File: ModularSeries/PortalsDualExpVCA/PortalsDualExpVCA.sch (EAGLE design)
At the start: 71 parts, among them Q1 2N3906, Q2 2N3906, Q3 2N3906, Q4 2N3906

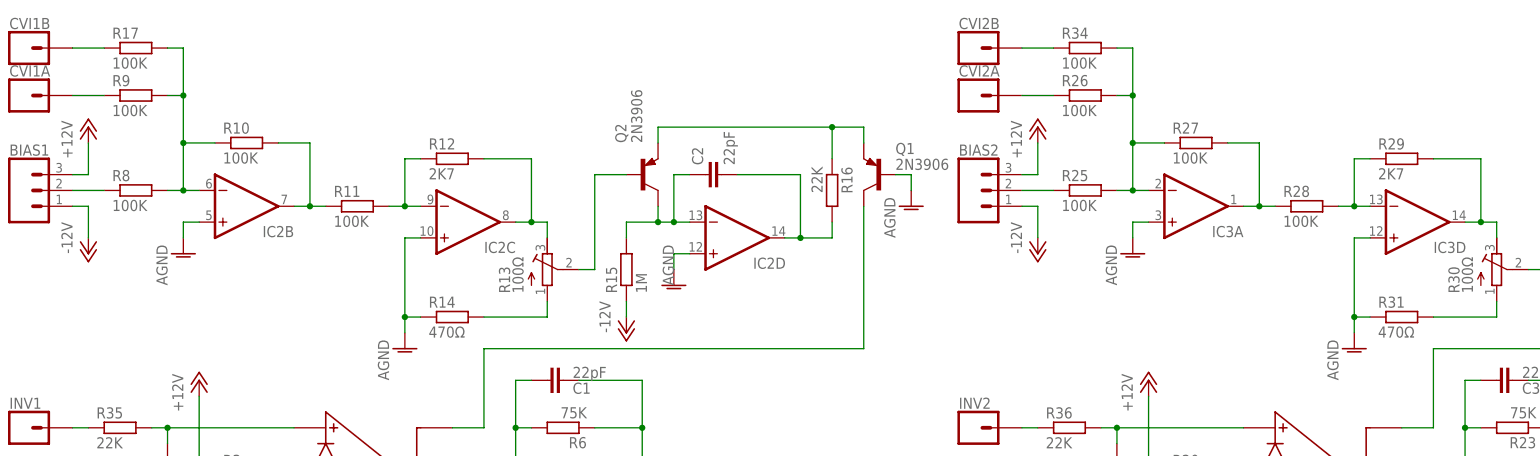
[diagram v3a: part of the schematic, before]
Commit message: Control PCBs for Prism, Portals, TimeSeeds and Knives added
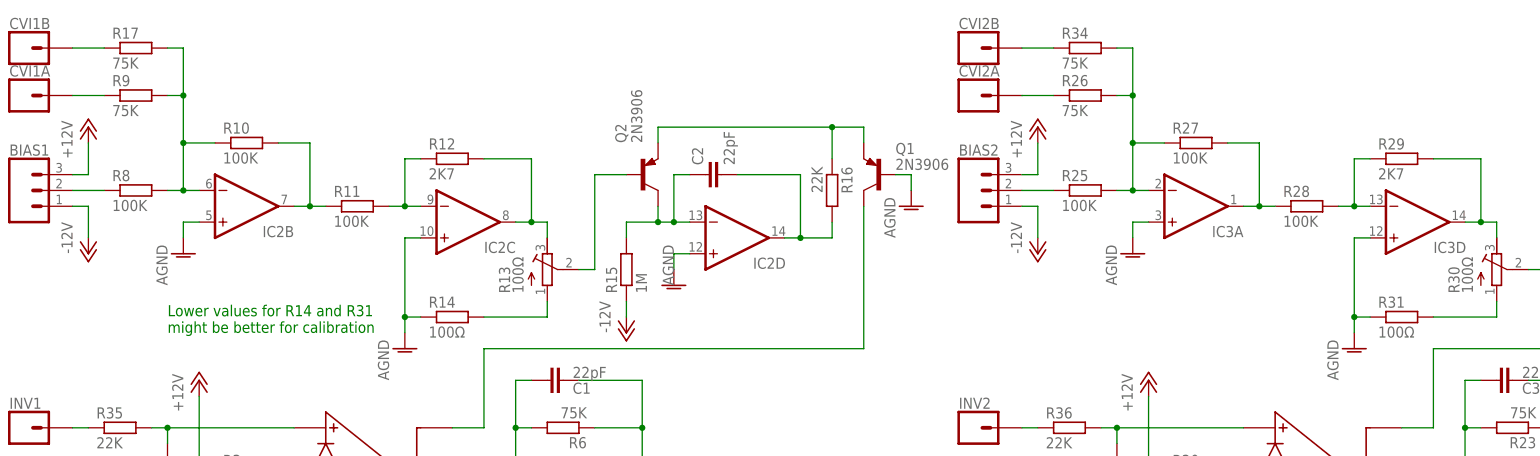
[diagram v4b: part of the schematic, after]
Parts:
- R14, R31: value 470Ω -> 100Ω
- R17, R26, R34, R9: value 100K -> 75K
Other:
- note added: "Lower values for R14 and R31 might be better for calibration"
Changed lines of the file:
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@@
 <part name="CVI1A" library="ElectricNoodleBox" deviceset="1XWIREPAD" device=""/>
 <part name="R8" library="rcl" library_urn="urn:adsk.eagle:library:334" deviceset="R-EU_" device="0207/10" package3d_urn="urn:adsk.eagle:package:23491/2" value="100K"/>
-<part name="R9" library="rcl" library_urn="urn:adsk.eagle:library:334" deviceset="R-EU_" device="0207/10" package3d_urn="urn:adsk.eagle:package:23491/2" value="100K"/>
+<part name="R9" library="rcl" library_urn="urn:adsk.eagle:library:334" deviceset="R-EU_" device="0207/10" package3d_urn="urn:adsk.eagle:package:23491/2" value="75K"/>
 <part name="R10" library="rcl" library_urn="urn:adsk.eagle:library:334" deviceset="R-EU_" device="0207/10" package3d_urn="urn:adsk.eagle:package:23491/2" value="100K"/>
 <part name="R11" library="rcl" library_urn="urn:adsk.eagle:library:334" deviceset="R-EU_" device="0207/10" package3d_urn="urn:adsk.eagle:package:23491/2" value="100K"/>
@@
 <part name="AGND5" library="supply1" library_urn="urn:adsk.eagle:library:371" deviceset="AGND" device=""/>
 <part name="R13" library="rcl" library_urn="urn:adsk.eagle:library:334" deviceset="R-TRIMM" device="3296W" package3d_urn="urn:adsk.eagle:package:26033/1" value="100Ω"/>
-<part name="R14" library="rcl" library_urn="urn:adsk.eagle:library:334" deviceset="R-EU_" device="0207/10" package3d_urn="urn:adsk.eagle:package:23491/2" value="470Ω"/>
+<part name="R14" library="rcl" library_urn="urn:adsk.eagle:library:334" deviceset="R-EU_" device="0207/10" package3d_urn="urn:adsk.eagle:package:23491/2" value="100Ω"/>
 <part name="AGND6" library="supply1" library_urn="urn:adsk.eagle:library:371" deviceset="AGND" device=""/>
 <part name="R15" library="rcl" library_urn="urn:adsk.eagle:library:334" deviceset="R-EU_" device="0207/10" package3d_urn="urn:adsk.eagle:package:23491/2" value="1M"/>
@@
 <part name="P+3" library="supply1" library_urn="urn:adsk.eagle:library:371" deviceset="+12V" device=""/>
 <part name="P-3" library="supply1" library_urn="urn:adsk.eagle:library:371" deviceset="-12V" device=""/>
-<part name="R17" library="rcl" library_urn="urn:adsk.eagle:library:334" deviceset="R-EU_" device="0207/10" package3d_urn="urn:adsk.eagle:package:23491/2" value="100K"/>
+<part name="R17" library="rcl" library_urn="urn:adsk.eagle:library:334" deviceset="R-EU_" device="0207/10" package3d_urn="urn:adsk.eagle:package:23491/2" value="75K"/>
 <part name="CVI1B" library="ElectricNoodleBox" deviceset="1XWIREPAD" device=""/>
 <part name="SI2" library="ElectricNoodleBox" deviceset="1XWIREPAD" device=""/>
@@
 <part name="CVI2A" library="ElectricNoodleBox" deviceset="1XWIREPAD" device=""/>
 <part name="R25" library="rcl" library_urn="urn:adsk.eagle:library:334" deviceset="R-EU_" device="0207/10" package3d_urn="urn:adsk.eagle:package:23491/2" value="100K"/>
-<part name="R26" library="rcl" library_urn="urn:adsk.eagle:library:334" deviceset="R-EU_" device="0207/10" package3d_urn="urn:adsk.eagle:package:23491/2" value="100K"/>
+<part name="R26" library="rcl" library_urn="urn:adsk.eagle:library:334" deviceset="R-EU_" device="0207/10" package3d_urn="urn:adsk.eagle:package:23491/2" value="75K"/>
 <part name="R27" library="rcl" library_urn="urn:adsk.eagle:library:334" deviceset="R-EU_" device="0207/10" package3d_urn="urn:adsk.eagle:package:23491/2" value="100K"/>
 <part name="R28" library="rcl" library_urn="urn:adsk.eagle:library:334" deviceset="R-EU_" device="0207/10" package3d_urn="urn:adsk.eagle:package:23491/2" value="100K"/>
@@
 <part name="AGND11" library="supply1" library_urn="urn:adsk.eagle:library:371" deviceset="AGND" device=""/>
 <part name="R30" library="rcl" library_urn="urn:adsk.eagle:library:334" deviceset="R-TRIMM" device="3296W" package3d_urn="urn:adsk.eagle:package:26033/1" value="100Ω"/>
-<part name="R31" library="rcl" library_urn="urn:adsk.eagle:library:334" deviceset="R-EU_" device="0207/10" package3d_urn="urn:adsk.eagle:package:23491/2" value="470Ω"/>
+<part name="R31" library="rcl" library_urn="urn:adsk.eagle:library:334" deviceset="R-EU_" device="0207/10" package3d_urn="urn:adsk.eagle:package:23491/2" value="100Ω"/>
 <part name="AGND12" library="supply1" library_urn="urn:adsk.eagle:library:371" deviceset="AGND" device=""/>
 <part name="R32" library="rcl" library_urn="urn:adsk.eagle:library:334" deviceset="R-EU_" device="0207/10" package3d_urn="urn:adsk.eagle:package:23491/2" value="1M"/>
@@
 <part name="P+5" library="supply1" library_urn="urn:adsk.eagle:library:371" deviceset="+12V" device=""/>
 <part name="P-5" library="supply1" library_urn="urn:adsk.eagle:library:371" deviceset="-12V" device=""/>
-<part name="R34" library="rcl" library_urn="urn:adsk.eagle:library:334" deviceset="R-EU_" device="0207/10" package3d_urn="urn:adsk.eagle:package:23491/2" value="100K"/>
+<part name="R34" library="rcl" library_urn="urn:adsk.eagle:library:334" deviceset="R-EU_" device="0207/10" package3d_urn="urn:adsk.eagle:package:23491/2" value="75K"/>
 <part name="CVI2B" library="ElectricNoodleBox" deviceset="1XWIREPAD" device=""/>
 <part name="C5" library="rcl" library_urn="urn:adsk.eagle:library:334" deviceset="C-EU" device="050-025X075" package3d_urn="urn:adsk.eagle:package:23637/1" value="100nF"/>
@@
 <text x="177.8" y="22.86" size="1.778" layer="91">Ground terminals
 for jacks / pots</text>
+<text x="30.48" y="88.9" size="1.778" layer="91">Lower values for R14 and R31
+might be better for calibration</text>
 </plain>
 <instances>

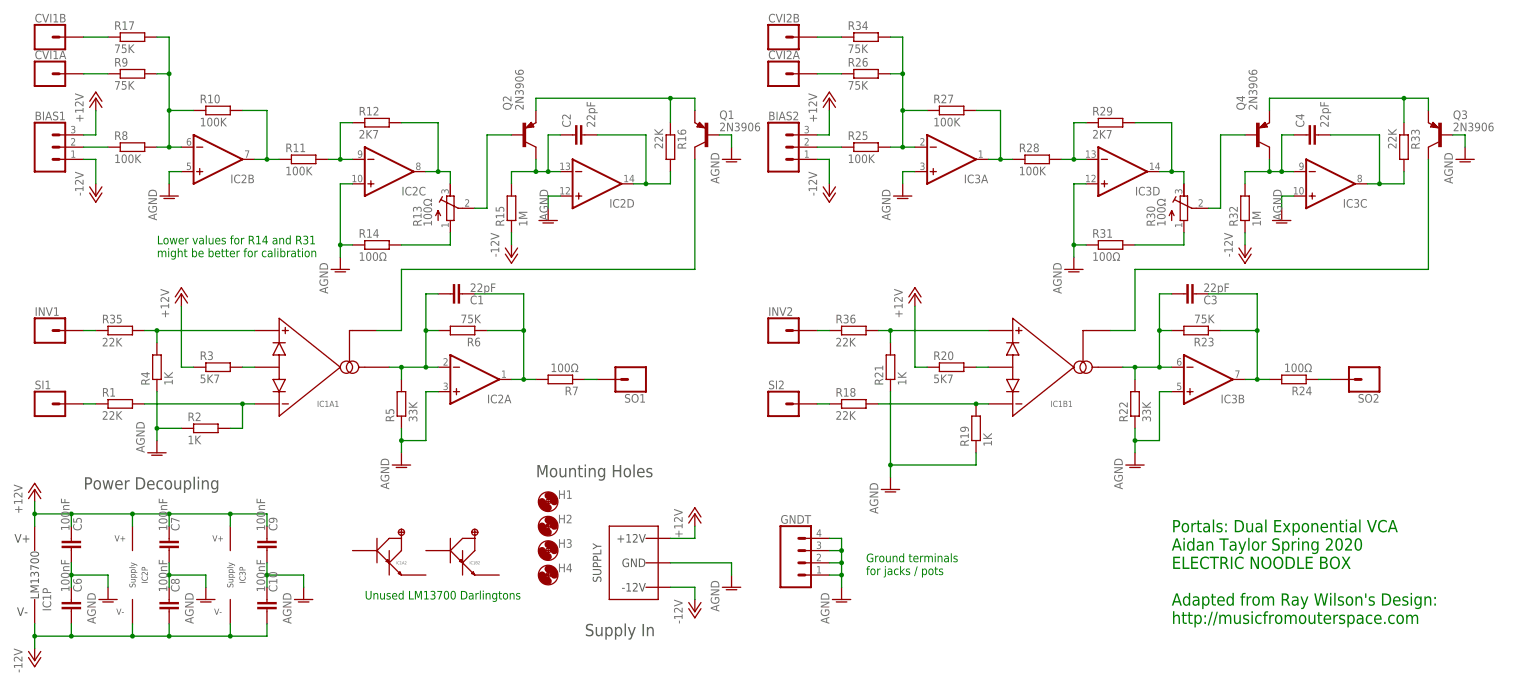
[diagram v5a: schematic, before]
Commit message: Updates to Portals and Knives, Panel layout for Prism and Knives added
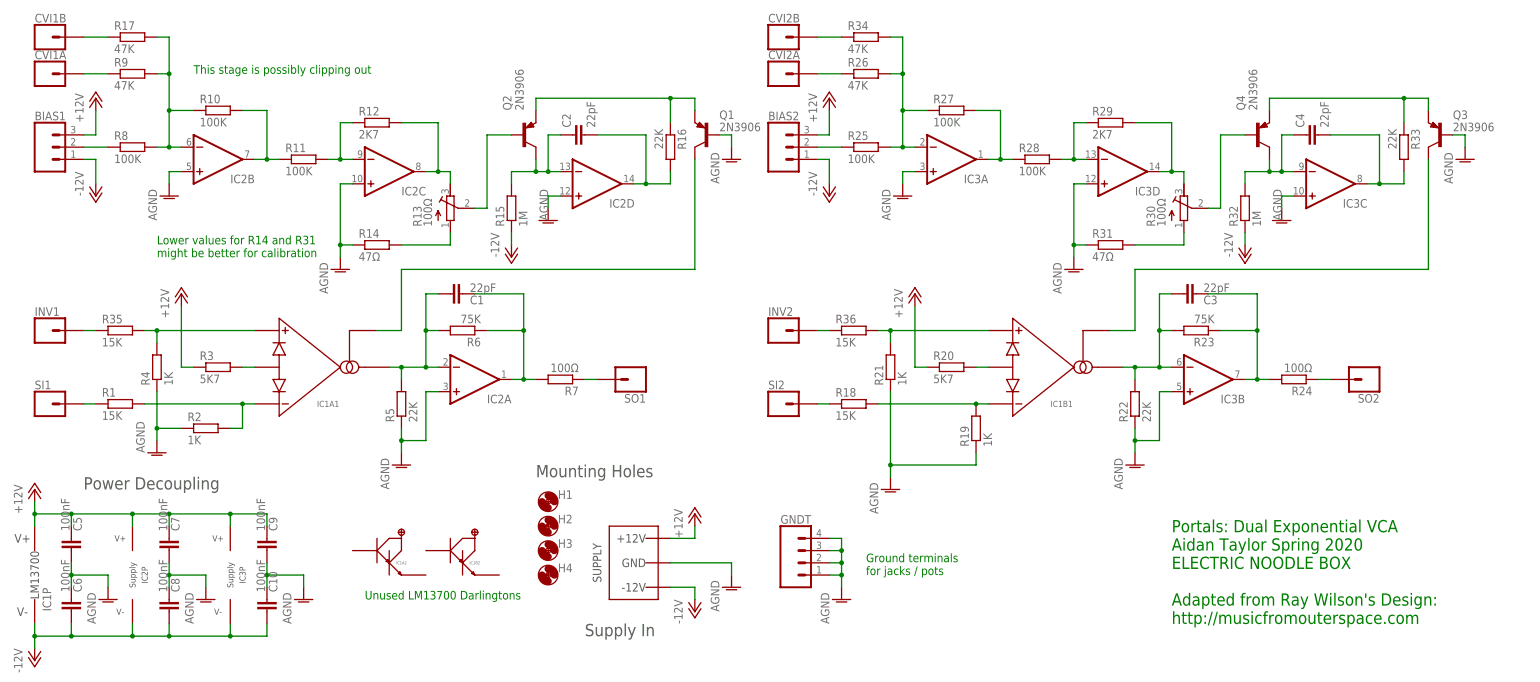
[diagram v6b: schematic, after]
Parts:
- R1, R18, R35, R36: value 22K -> 15K
- R14, R31: value 100Ω -> 47Ω
- R17, R26, R34, R9: value 75K -> 47K
- R22, R5: value 33K -> 22K
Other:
- note added: "This stage is possibly clipping out"
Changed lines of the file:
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@@
 <?xml version="1.0" encoding="utf-8"?>
 <!DOCTYPE eagle SYSTEM "eagle.dtd">
-<eagle version="9.6.2">
+<eagle version="9.6.0">
 <drawing>
 <settings>
@@
 <part name="IC1" library="ElectricNoodleBox" deviceset="LM13700" device="DIL" package3d_urn="urn:adsk.eagle:package:922/2"/>
 <part name="SI1" library="ElectricNoodleBox" deviceset="1XWIREPAD" device=""/>
-<part name="R1" library="rcl" library_urn="urn:adsk.eagle:library:334" deviceset="R-EU_" device="0207/10" package3d_urn="urn:adsk.eagle:package:23491/2" value="22K"/>
+<part name="R1" library="rcl" library_urn="urn:adsk.eagle:library:334" deviceset="R-EU_" device="0207/10" package3d_urn="urn:adsk.eagle:package:23491/2" value="15K"/>
 <part name="R2" library="rcl" library_urn="urn:adsk.eagle:library:334" deviceset="R-EU_" device="0207/10" package3d_urn="urn:adsk.eagle:package:23491/2" value="1K"/>
 <part name="R3" library="rcl" library_urn="urn:adsk.eagle:library:334" deviceset="R-EU_" device="0207/10" package3d_urn="urn:adsk.eagle:package:23491/2" value="5K7"/>
 <part name="R4" library="rcl" library_urn="urn:adsk.eagle:library:334" deviceset="R-EU_" device="0207/10" package3d_urn="urn:adsk.eagle:package:23491/2" value="1K"/>
-<part name="R5" library="rcl" library_urn="urn:adsk.eagle:library:334" deviceset="R-EU_" device="0207/10" package3d_urn="urn:adsk.eagle:package:23491/2" value="33K"/>
+<part name="R5" library="rcl" library_urn="urn:adsk.eagle:library:334" deviceset="R-EU_" device="0207/10" package3d_urn="urn:adsk.eagle:package:23491/2" value="22K"/>
 <part name="IC2" library="ElectricNoodleBox" deviceset="TL0X4" device="DIL" package3d_urn="urn:adsk.eagle:package:16407/2"/>
 <part name="P+1" library="supply1" library_urn="urn:adsk.eagle:library:371" deviceset="+12V" device=""/>
@@
 <part name="CVI1A" library="ElectricNoodleBox" deviceset="1XWIREPAD" device=""/>
 <part name="R8" library="rcl" library_urn="urn:adsk.eagle:library:334" deviceset="R-EU_" device="0207/10" package3d_urn="urn:adsk.eagle:package:23491/2" value="100K"/>
-<part name="R9" library="rcl" library_urn="urn:adsk.eagle:library:334" deviceset="R-EU_" device="0207/10" package3d_urn="urn:adsk.eagle:package:23491/2" value="75K"/>
+<part name="R9" library="rcl" library_urn="urn:adsk.eagle:library:334" deviceset="R-EU_" device="0207/10" package3d_urn="urn:adsk.eagle:package:23491/2" value="47K"/>
 <part name="R10" library="rcl" library_urn="urn:adsk.eagle:library:334" deviceset="R-EU_" device="0207/10" package3d_urn="urn:adsk.eagle:package:23491/2" value="100K"/>
 <part name="R11" library="rcl" library_urn="urn:adsk.eagle:library:334" deviceset="R-EU_" device="0207/10" package3d_urn="urn:adsk.eagle:package:23491/2" value="100K"/>
@@
 <part name="AGND5" library="supply1" library_urn="urn:adsk.eagle:library:371" deviceset="AGND" device=""/>
 <part name="R13" library="rcl" library_urn="urn:adsk.eagle:library:334" deviceset="R-TRIMM" device="3296W" package3d_urn="urn:adsk.eagle:package:26033/1" value="100Ω"/>
-<part name="R14" library="rcl" library_urn="urn:adsk.eagle:library:334" deviceset="R-EU_" device="0207/10" package3d_urn="urn:adsk.eagle:package:23491/2" value="100Ω"/>
+<part name="R14" library="rcl" library_urn="urn:adsk.eagle:library:334" deviceset="R-EU_" device="0207/10" package3d_urn="urn:adsk.eagle:package:23491/2" value="47Ω"/>
 <part name="AGND6" library="supply1" library_urn="urn:adsk.eagle:library:371" deviceset="AGND" device=""/>
 <part name="R15" library="rcl" library_urn="urn:adsk.eagle:library:334" deviceset="R-EU_" device="0207/10" package3d_urn="urn:adsk.eagle:package:23491/2" value="1M"/>
@@
 <part name="P+3" library="supply1" library_urn="urn:adsk.eagle:library:371" deviceset="+12V" device=""/>
 <part name="P-3" library="supply1" library_urn="urn:adsk.eagle:library:371" deviceset="-12V" device=""/>
-<part name="R17" library="rcl" library_urn="urn:adsk.eagle:library:334" deviceset="R-EU_" device="0207/10" package3d_urn="urn:adsk.eagle:package:23491/2" value="75K"/>
+<part name="R17" library="rcl" library_urn="urn:adsk.eagle:library:334" deviceset="R-EU_" device="0207/10" package3d_urn="urn:adsk.eagle:package:23491/2" value="47K"/>
 <part name="CVI1B" library="ElectricNoodleBox" deviceset="1XWIREPAD" device=""/>
 <part name="SI2" library="ElectricNoodleBox" deviceset="1XWIREPAD" device=""/>
-<part name="R18" library="rcl" library_urn="urn:adsk.eagle:library:334" deviceset="R-EU_" device="0207/10" package3d_urn="urn:adsk.eagle:package:23491/2" value="22K"/>
+<part name="R18" library="rcl" library_urn="urn:adsk.eagle:library:334" deviceset="R-EU_" device="0207/10" package3d_urn="urn:adsk.eagle:package:23491/2" value="15K"/>
 <part name="R19" library="rcl" library_urn="urn:adsk.eagle:library:334" deviceset="R-EU_" device="0207/10" package3d_urn="urn:adsk.eagle:package:23491/2" value="1K"/>
 <part name="R20" library="rcl" library_urn="urn:adsk.eagle:library:334" deviceset="R-EU_" device="0207/10" package3d_urn="urn:adsk.eagle:package:23491/2" value="5K7"/>
 <part name="R21" library="rcl" library_urn="urn:adsk.eagle:library:334" deviceset="R-EU_" device="0207/10" package3d_urn="urn:adsk.eagle:package:23491/2" value="1K"/>
-<part name="R22" library="rcl" library_urn="urn:adsk.eagle:library:334" deviceset="R-EU_" device="0207/10" package3d_urn="urn:adsk.eagle:package:23491/2" value="33K"/>
+<part name="R22" library="rcl" library_urn="urn:adsk.eagle:library:334" deviceset="R-EU_" device="0207/10" package3d_urn="urn:adsk.eagle:package:23491/2" value="22K"/>
 <part name="IC3" library="ElectricNoodleBox" deviceset="TL0X4" device="DIL" package3d_urn="urn:adsk.eagle:package:16407/2"/>
 <part name="C3" library="rcl" library_urn="urn:adsk.eagle:library:334" deviceset="C-EU" device="050-025X075" package3d_urn="urn:adsk.eagle:package:23637/1" value="22pF"/>
@@
 <part name="CVI2A" library="ElectricNoodleBox" deviceset="1XWIREPAD" device=""/>
 <part name="R25" library="rcl" library_urn="urn:adsk.eagle:library:334" deviceset="R-EU_" device="0207/10" package3d_urn="urn:adsk.eagle:package:23491/2" value="100K"/>
-<part name="R26" library="rcl" library_urn="urn:adsk.eagle:library:334" deviceset="R-EU_" device="0207/10" package3d_urn="urn:adsk.eagle:package:23491/2" value="75K"/>
+<part name="R26" library="rcl" library_urn="urn:adsk.eagle:library:334" deviceset="R-EU_" device="0207/10" package3d_urn="urn:adsk.eagle:package:23491/2" value="47K"/>
 <part name="R27" library="rcl" library_urn="urn:adsk.eagle:library:334" deviceset="R-EU_" device="0207/10" package3d_urn="urn:adsk.eagle:package:23491/2" value="100K"/>
 <part name="R28" library="rcl" library_urn="urn:adsk.eagle:library:334" deviceset="R-EU_" device="0207/10" package3d_urn="urn:adsk.eagle:package:23491/2" value="100K"/>
@@
 <part name="AGND11" library="supply1" library_urn="urn:adsk.eagle:library:371" deviceset="AGND" device=""/>
 <part name="R30" library="rcl" library_urn="urn:adsk.eagle:library:334" deviceset="R-TRIMM" device="3296W" package3d_urn="urn:adsk.eagle:package:26033/1" value="100Ω"/>
-<part name="R31" library="rcl" library_urn="urn:adsk.eagle:library:334" deviceset="R-EU_" device="0207/10" package3d_urn="urn:adsk.eagle:package:23491/2" value="100Ω"/>
+<part name="R31" library="rcl" library_urn="urn:adsk.eagle:library:334" deviceset="R-EU_" device="0207/10" package3d_urn="urn:adsk.eagle:package:23491/2" value="47Ω"/>
 <part name="AGND12" library="supply1" library_urn="urn:adsk.eagle:library:371" deviceset="AGND" device=""/>
 <part name="R32" library="rcl" library_urn="urn:adsk.eagle:library:334" deviceset="R-EU_" device="0207/10" package3d_urn="urn:adsk.eagle:package:23491/2" value="1M"/>
@@
 <part name="P+5" library="supply1" library_urn="urn:adsk.eagle:library:371" deviceset="+12V" device=""/>
 <part name="P-5" library="supply1" library_urn="urn:adsk.eagle:library:371" deviceset="-12V" device=""/>
-<part name="R34" library="rcl" library_urn="urn:adsk.eagle:library:334" deviceset="R-EU_" device="0207/10" package3d_urn="urn:adsk.eagle:package:23491/2" value="75K"/>
+<part name="R34" library="rcl" library_urn="urn:adsk.eagle:library:334" deviceset="R-EU_" device="0207/10" package3d_urn="urn:adsk.eagle:package:23491/2" value="47K"/>
 <part name="CVI2B" library="ElectricNoodleBox" deviceset="1XWIREPAD" device=""/>
 <part name="C5" library="rcl" library_urn="urn:adsk.eagle:library:334" deviceset="C-EU" device="050-025X075" package3d_urn="urn:adsk.eagle:package:23637/1" value="100nF"/>
@@
 <part name="INV1" library="ElectricNoodleBox" deviceset="1XWIREPAD" device=""/>
 <part name="INV2" library="ElectricNoodleBox" deviceset="1XWIREPAD" device=""/>
-<part name="R35" library="rcl" library_urn="urn:adsk.eagle:library:334" deviceset="R-EU_" device="0207/10" package3d_urn="urn:adsk.eagle:package:23491/2" value="22K"/>
-<part name="R36" library="rcl" library_urn="urn:adsk.eagle:library:334" deviceset="R-EU_" device="0207/10" package3d_urn="urn:adsk.eagle:package:23491/2" value="22K"/>
+<part name="R35" library="rcl" library_urn="urn:adsk.eagle:library:334" deviceset="R-EU_" device="0207/10" package3d_urn="urn:adsk.eagle:package:23491/2" value="15K"/>
+<part name="R36" library="rcl" library_urn="urn:adsk.eagle:library:334" deviceset="R-EU_" device="0207/10" package3d_urn="urn:adsk.eagle:package:23491/2" value="15K"/>
 <part name="GNDT" library="ElectricNoodleBox" deviceset="4XWIREPAD" device=""/>
 <part name="AGND16" library="supply1" library_urn="urn:adsk.eagle:library:371" deviceset="AGND" device=""/>
@@
 <text x="30.48" y="88.9" size="1.778" layer="91">Lower values for R14 and R31
 might be better for calibration</text>
+<text x="38.1" y="127" size="1.778" layer="91">This stage is possibly clipping out</text>
 </plain>
 <instances>
